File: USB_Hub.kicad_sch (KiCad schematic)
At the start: 48 parts, among them U4 VL822-QFN76, U5 AP7331-10WG-7, Y1 25MHz

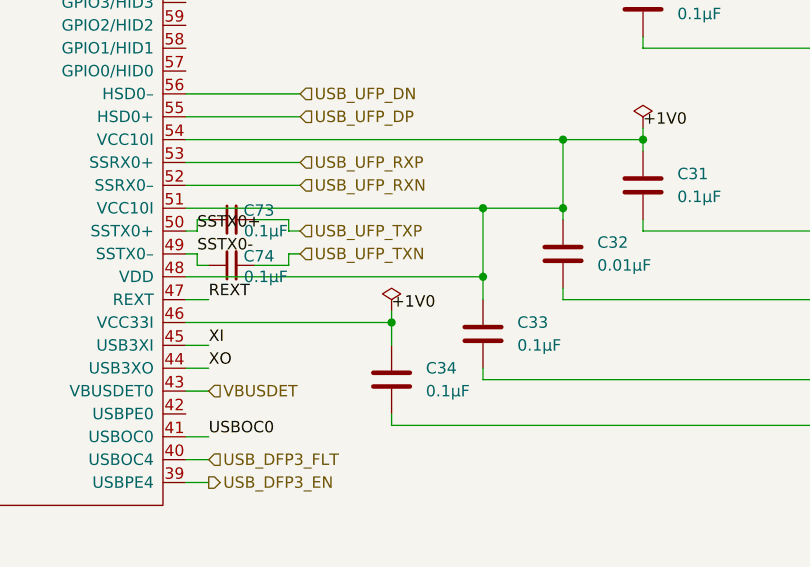
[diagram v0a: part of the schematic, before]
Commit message: Fixed USB Hub wrong net 1V0 -> 3V3
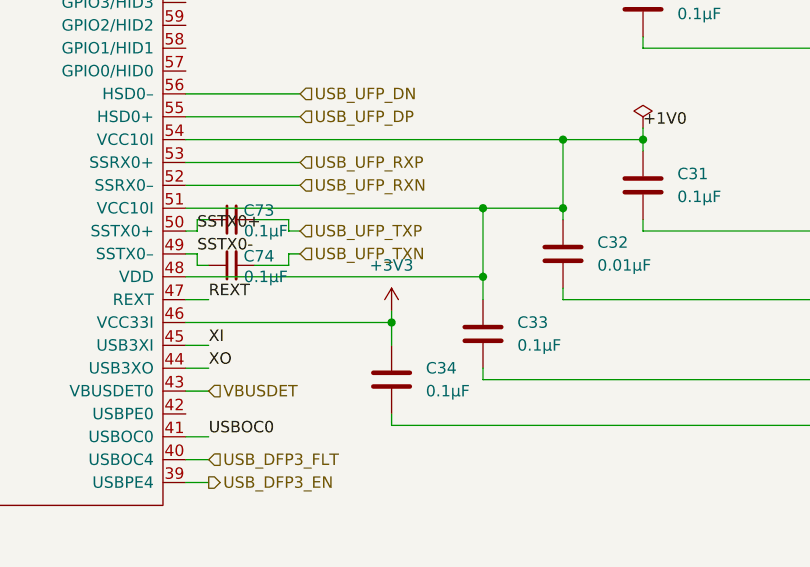
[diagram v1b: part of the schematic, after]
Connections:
- net +1V0: no longer C34.1, U4.46 (VCC33I)
- net +3V3: now also C34.1, U4.46 (VCC33I)
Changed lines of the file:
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@@
 	(wire
 		(pts
-			(xy 175.26 22.86) (xy 177.8 22.86)
-		)
-		(stroke
-			(width 0)
-			(type default)
-		)
-	)
-	(wire
-		(pts
 			(xy 110.49 52.07) (xy 111.76 52.07)
 		)
@@
 	(wire
 		(pts
+			(xy 175.26 22.86) (xy 177.8 22.86)
+		)
+		(stroke
+			(width 0)
+			(type default)
+		)
+	)
+	(wire
+		(pts
 			(xy 175.26 73.66) (xy 187.96 73.66)
 		)
@@
 	)
 	(label "+1V0"
-		(at 198.12 95.25 0)
-		(fields_autoplaced yes)
-		(effects
-			(font
-				(size 1.27 1.27)
-			)
-			(justify left bottom)
-		)
-	)
-	(label "+1V0"
 		(at 20.32 26.67 0)
 		(fields_autoplaced yes)
@@
 		)
 	)
-	(label "USB_DFP3_FLT"
-		(at 166.37 194.31 180)
-		(fields_autoplaced yes)
-		(effects
-			(font
-				(size 1.27 1.27)
-			)
-			(justify right bottom)
-		)
-	)
 	(label "USB_DFP1_FLT"
 		(at 148.59 189.23 180)
@@
 		)
 	)
+	(label "USB_DFP3_FLT"
+		(at 166.37 194.31 180)
+		(fields_autoplaced yes)
+		(effects
+			(font
+				(size 1.27 1.27)
+			)
+			(justify right bottom)
+		)
+	)
 	(label "+1V0"
 		(at 76.2 85.09 0)
@@
 		)
 	)
+	(hierarchical_label "USB_DFP1_FLT"
+		(shape input)
+		(at 177.8 22.86 0)
+		(fields_autoplaced yes)
+		(effects
+			(font
+				(size 1.27 1.27)
+			)
+			(justify left)
+		)
+	)
 	(hierarchical_label "SCL"
 		(shape bidirectional)
@@
 		)
 	)
-	(hierarchical_label "USB_DFP1_FLT"
-		(shape input)
-		(at 177.8 22.86 0)
-		(fields_autoplaced yes)
-		(effects
-			(font
-				(size 1.27 1.27)
-			)
-			(justify left)
-		)
-	)
 	(hierarchical_label "SDA"
 		(shape bidirectional)
@@
 	)
 	(symbol
+		(lib_id "power:+3V3")
+		(at 198.12 95.25 0)
+		(unit 1)
+		(exclude_from_sim no)
+		(in_bom yes)
+		(on_board yes)
+		(dnp no)
+		(fields_autoplaced yes)
+		(property "Reference" "#PWR0129"
+			(at 198.12 99.06 0)
+			(effects
+				(font
+					(size 1.27 1.27)
+				)
+				(hide yes)
+			)
+		)
+		(property "Value" "+3V3"
+			(at 198.12 90.17 0)
+			(effects
+				(font
+					(size 1.27 1.27)
+				)
+			)
+		)
+		(property "Footprint" ""
+			(at 198.12 95.25 0)
+			(effects
+				(font
+					(size 1.27 1.27)
+				)
+				(hide yes)
+			)
+		)
+		(property "Datasheet" ""
+			(at 198.12 95.25 0)
+			(effects
+				(font
+					(size 1.27 1.27)
+				)
+				(hide yes)
+			)
+		)
+		(property "Description" "Power symbol creates a global label with name \"+3V3\""
+			(at 198.12 95.25 0)
+			(effects
+				(font
+					(size 1.27 1.27)
+				)
+				(hide yes)
+			)
+		)
+		(pin "1"
+		)
+		(instances
+			(project "XG_Mobile_Dock"
+				(path "/f97e6956-ab08-42cb-8fed-03fa58e87f0e/ef21a87f-222f-4a81-a291-59975487be1d"
+					(reference "#PWR0129")
+					(unit 1)
+				)
+			)
+		)
+	)
+	(symbol
 		(lib_id "Device:R")
 		(at 266.7 58.42 180)
@@
 					(unit 1)
 				)
-			)
-		)
-	)
-	(symbol
-		(lib_id "power:PWR_FLAG")
-		(at 198.12 95.25 0)
-		(unit 1)
-		(exclude_from_sim no)
-		(in_bom yes)
-		(on_board yes)
-		(dnp no)
-		(fields_autoplaced yes)
-		(property "Reference" "#FLG09"
-			(at 198.12 93.345 0)
-			(effects
-				(font
-					(size 1.27 1.27)
-				)
-				(hide yes)
-			)
-		)
-		(property "Value" "PWR_FLAG"
-			(at 198.12 90.17 0)
-			(effects
-				(font
-					(size 1.27 1.27)
-				)
-				(hide yes)
-			)
-		)
-		(property "Footprint" ""
-			(at 198.12 95.25 0)
-			(effects
-				(font
-					(size 1.27 1.27)
-				)
-				(hide yes)
-			)
-		)
-		(property "Datasheet" "~"
-			(at 198.12 95.25 0)
-			(effects
-				(font
-					(size 1.27 1.27)
-				)
-				(hide yes)
-			)
-		)
-		(property "Description" "Special symbol for telling ERC where power comes from"
-			(at 198.12 95.25 0)
-			(effects
-				(font
-					(size 1.27 1.27)
-				)
-				(hide yes)
-			)
-		)
-		(pin "1"
-		)
-		(instances
-			(project "XG_Mobile_Dock"
-				(path "/f97e6956-ab08-42cb-8fed-03fa58e87f0e/ef21a87f-222f-4a81-a291-59975487be1d"
-					(reference "#FLG09")
-					(unit 1)
-				)

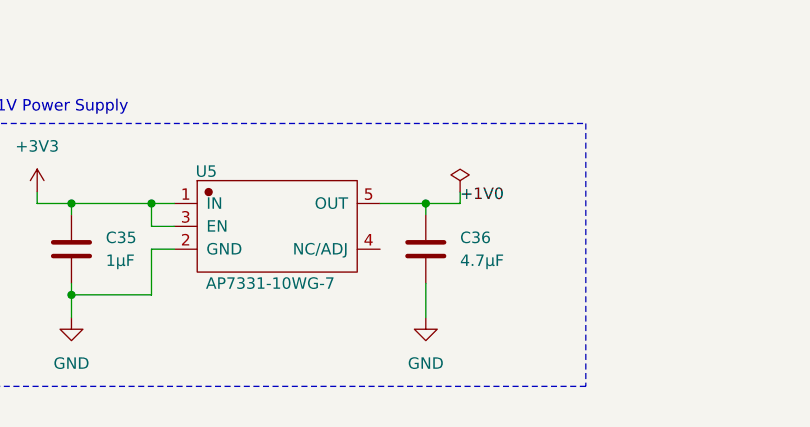
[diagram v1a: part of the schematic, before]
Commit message: Increase thermal mass under 1V0 LDO
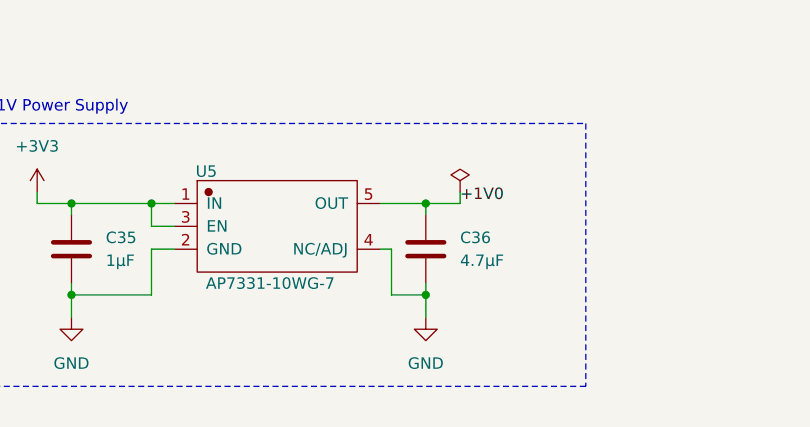
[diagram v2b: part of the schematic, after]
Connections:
- net GND: now also U5.4 (NC/ADJ)
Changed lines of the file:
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@@
 	)
 	(junction
+		(at 66.04 182.88)
+		(diameter 0)
+		(color 0 0 0 0)
+	)
+	(junction
 		(at 41.91 93.98)
 		(diameter 0)
@@
 	(wire
 		(pts
+			(xy 62.23 177.8) (xy 62.23 182.88)
+		)
+		(stroke
+			(width 0)
+			(type default)
+		)
+	)
+	(wire
+		(pts
 			(xy 41.91 109.22) (xy 41.91 110.49)
 		)
@@
 	(wire
 		(pts
-			(xy 66.04 181.61) (xy 66.04 185.42)
+			(xy 66.04 181.61) (xy 66.04 182.88)
 		)
 		(stroke
@@
 	(wire
 		(pts
+			(xy 62.23 182.88) (xy 66.04 182.88)
+		)
+		(stroke
+			(width 0)
+			(type default)
+		)
+	)
+	(wire
+		(pts
 			(xy 208.28 101.6) (xy 208.28 102.87)
 		)
@@
 	(wire
 		(pts
+			(xy 66.04 182.88) (xy 66.04 185.42)
+		)
+		(stroke
+			(width 0)
+			(type default)
+		)
+	)
+	(wire
+		(pts
 			(xy 166.37 173.99) (xy 157.48 173.99)
 		)
@@
 	(wire
 		(pts
+			(xy 60.96 177.8) (xy 62.23 177.8)
+		)
+		(stroke
+			(width 0)
+			(type default)
+		)
+	)
+	(wire
+		(pts
 			(xy 175.26 20.32) (xy 177.8 20.32)
 		)
@@
 		(on_board yes)
 		(dnp no)
-		(fields_autoplaced yes)
 		(property "Reference" "U5"
 			(at 41.656 169.164 0)

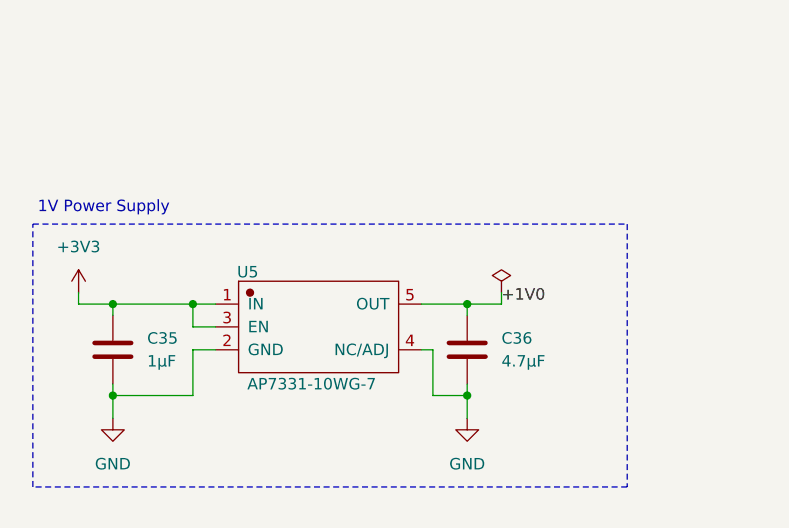
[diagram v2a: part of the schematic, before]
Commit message: Replace AP7331-10WG-7 with AP7361-10ER-13 to handle power draw
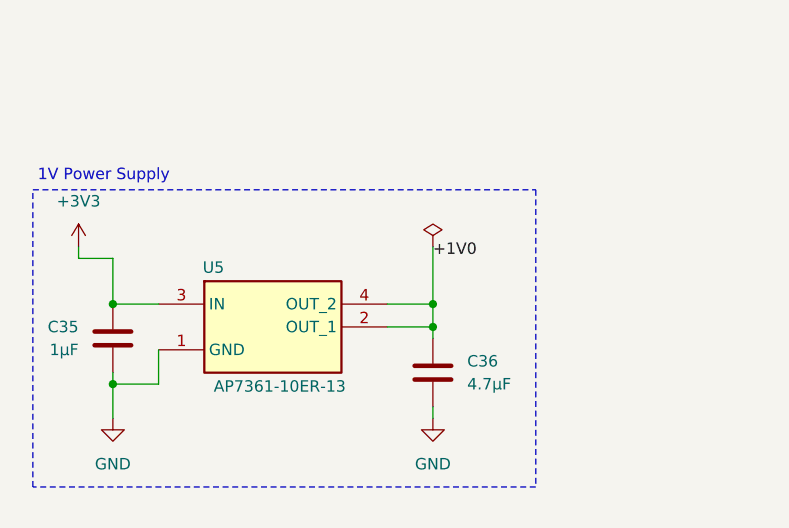
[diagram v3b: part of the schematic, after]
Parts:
- U5: value AP7331-10WG-7 -> AP7361-10ER-13; footprint AP7331-10WG-7:AP7331-10WG-7 -> AP7361-10ER-13:SOT230P700X180-4N; symbol AP7331-10WG-7:AP7331-10WG-7 -> AP7361-10ER-13:AP7361-10ER-13; Height (none) -> 1.8; LCSC C460375 -> C460389; Manufacturer_Name (none) -> Diodes Incorporated; Manufacturer_Part_Number (none) -> AP7361-10ER-13; Mouser Part Number (none) -> 621-AP7361-10ER-13; Mouser Price/Stock (none) -> https://www.mouser.co.uk/ProductDetail/Diodes-Incorporated/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; Part_Number AP7331-10WG-7 -> AP7361-10ER-13; uuid std:bcc43397ad83422c80ea21646716de2d -> (none)
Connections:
- net +1V0: now also U5.2 (OUT_1), U5.4 (OUT_2); no longer U5.5 (OUT)
- net +3V3: no longer U5.1 (IN)
- net GND: now also U5.1 (GND); no longer U5.2 (GND), U5.4 (NC/ADJ)
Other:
- moved on the sheet: C35, C36

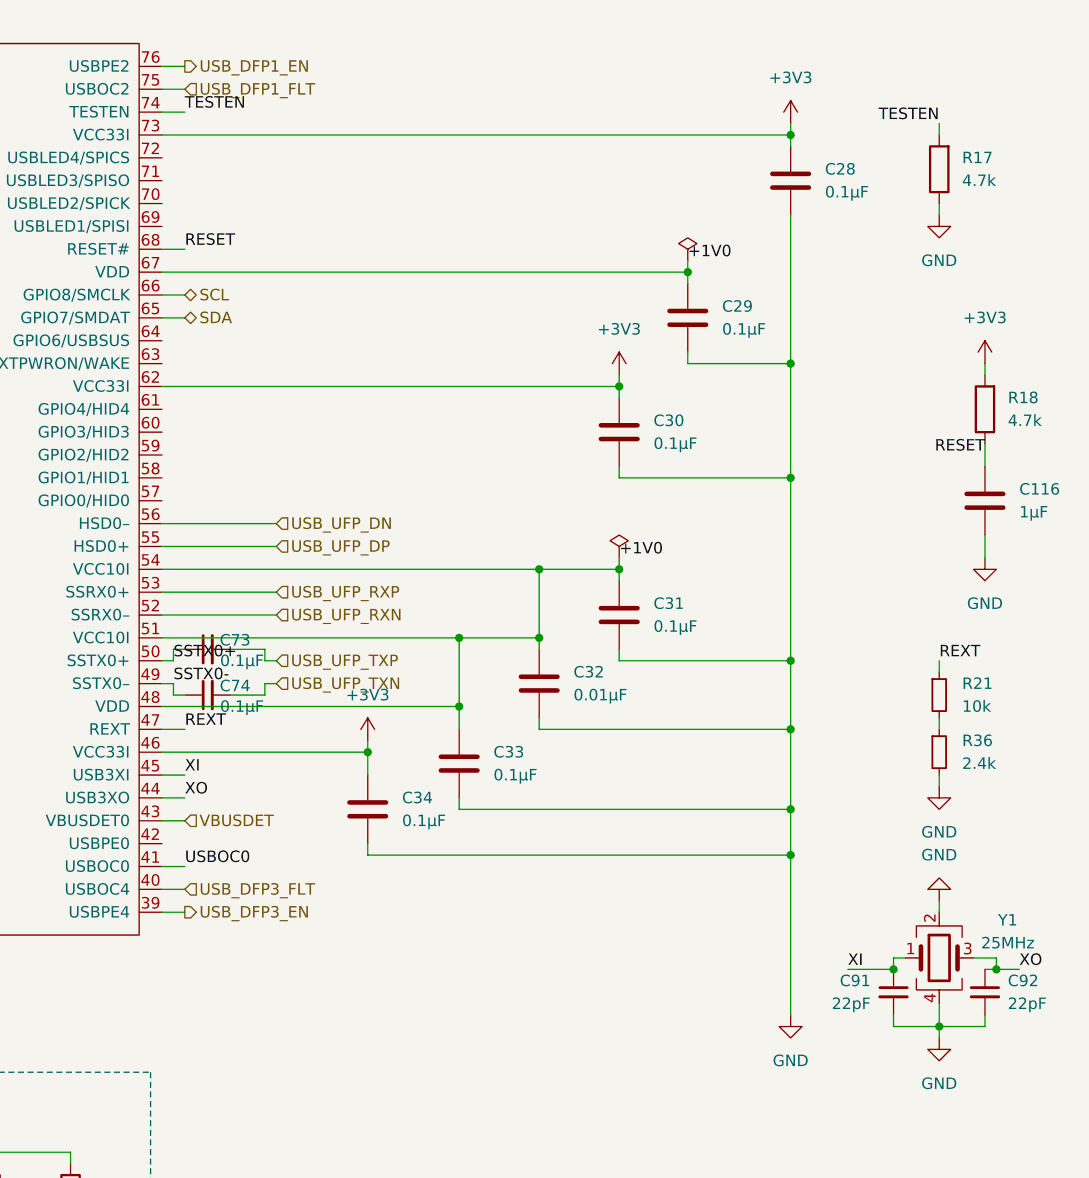
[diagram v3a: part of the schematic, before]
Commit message: pcb: redid layout for USB hub
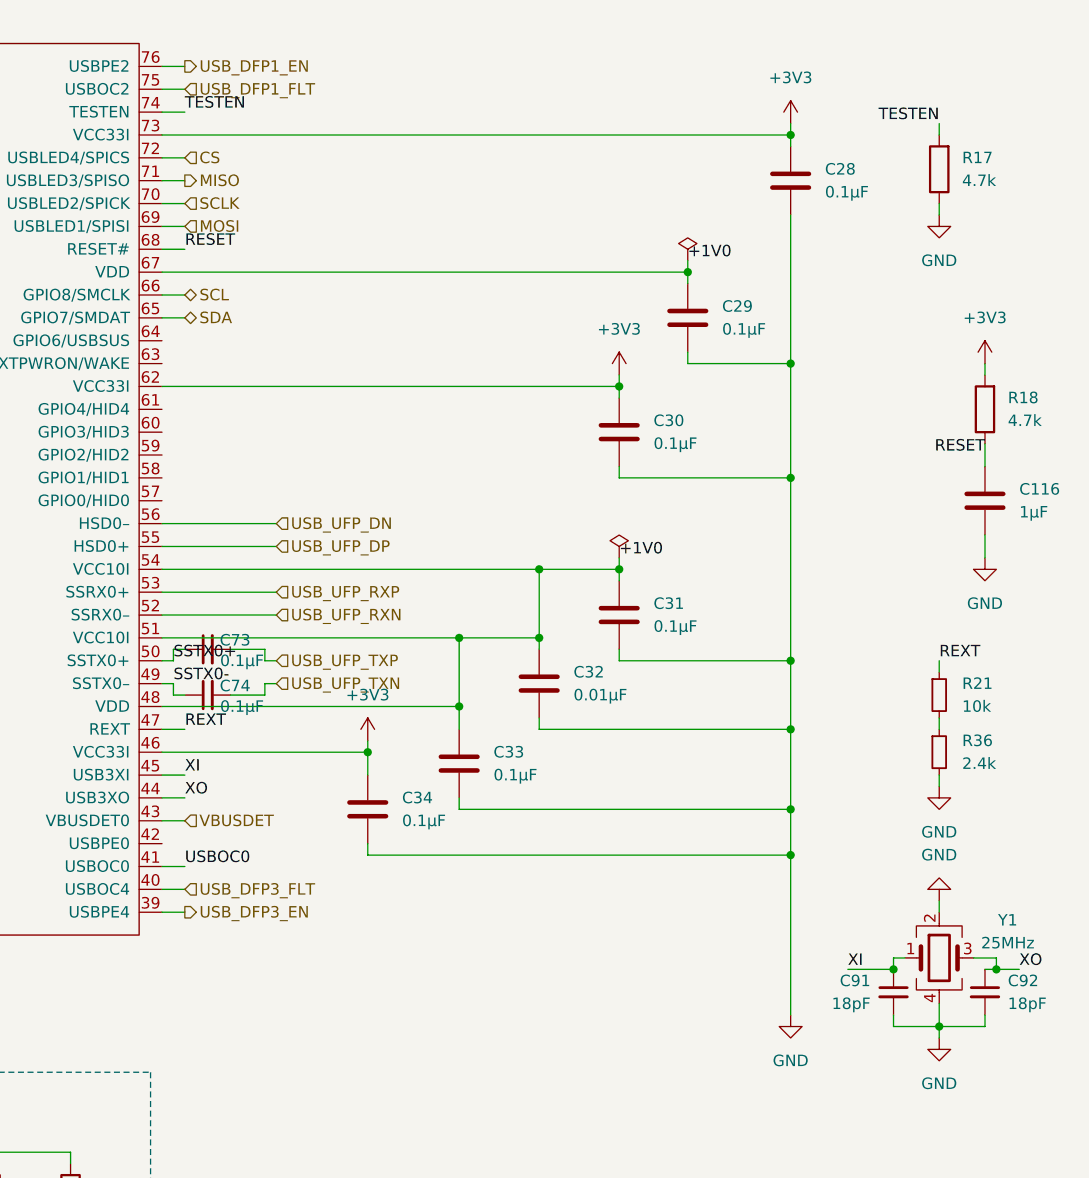
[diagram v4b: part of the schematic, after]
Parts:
- C91, C92: value 22pF -> 18pF; LCSC C1653 -> C1647; Part_Number CL10C220JB8NNNC -> CL10C180JB8NNNC
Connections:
- net MOSI: now reaches U4.69 (USBLED1/SPISI)
- net SCLK: now reaches U4.70 (USBLED2/SPICK)
- net MISO: now reaches U4.71 (USBLED3/SPISO)
- net CS: now reaches U4.72 (USBLED4/SPICS)
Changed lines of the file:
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@@
 	(wire
 		(pts
+			(xy 175.26 33.02) (xy 177.8 33.02)
+		)
+		(stroke
+			(width 0)
+			(type default)
+		)
+	)
+	(wire
+		(pts
 			(xy 156.21 149.86) (xy 156.21 156.21)
 		)
@@
 	(wire
 		(pts
+			(xy 175.26 38.1) (xy 177.8 38.1)
+		)
+		(stroke
+			(width 0)
+			(type default)
+		)
+	)
+	(wire
+		(pts
 			(xy 110.49 99.06) (xy 110.49 100.33)
 		)
@@
 	(wire
 		(pts
+			(xy 175.26 30.48) (xy 177.8 30.48)
+		)
+		(stroke
+			(width 0)
+			(type default)
+		)
+	)
+	(wire
+		(pts
 			(xy 175.26 78.74) (xy 187.96 78.74)
 		)
@@
 	(wire
 		(pts
+			(xy 175.26 35.56) (xy 177.8 35.56)
+		)
+		(stroke
+			(width 0)
+			(type default)
+		)
+	)
+	(wire
+		(pts
 			(xy 261.62 35.56) (xy 261.62 36.83)
 		)
@@
 		)
 	)
+	(hierarchical_label "SCLK"
+		(shape input)
+		(at 177.8 35.56 0)
+		(fields_autoplaced yes)
+		(effects
+			(font
+				(size 1.27 1.27)
+			)
+			(justify left)
+		)
+	)
 	(hierarchical_label "USB_DFP0_DN"
 		(shape input)
@@
 		)
 	)
+	(hierarchical_label "MISO"
+		(shape output)
+		(at 177.8 33.02 0)
+		(fields_autoplaced yes)
+		(effects
+			(font
+				(size 1.27 1.27)
+			)
+			(justify left)
+		)
+	)
+	(hierarchical_label "MOSI"
+		(shape input)
+		(at 177.8 38.1 0)
+		(fields_autoplaced yes)
+		(effects
+			(font
+				(size 1.27 1.27)
+			)
+			(justify left)
+		)
+	)
 	(hierarchical_label "USB_DFP1_DP"
 		(shape input)
@@
 		)
 	)
+	(hierarchical_label "CS"
+		(shape input)
+		(at 177.8 30.48 0)
+		(fields_autoplaced yes)
+		(effects
+			(font
+				(size 1.27 1.27)
+			)
+			(justify left)
+		)
+	)
 	(hierarchical_label "USB_DFP0_EN"
 		(shape output)
@@
 			)
 		)
-		(property "Value" "22pF"
+		(property "Value" "18pF"
 			(at 254 124.4662 0)
 			(effects
@@
 			)
 		)
-		(property "LCSC" "C1653"
+		(property "LCSC" "C1647"
 			(at 256.54 123.19 0)
 			(effects
@@
 			)
 		)
-		(property "Part_Number" "CL10C220JB8NNNC"
+		(property "Part_Number" "CL10C180JB8NNNC"
 			(at 256.54 123.19 0)
 			(effects
@@
 			)
 		)
-		(property "Value" "22pF"
+		(property "Value" "18pF"
 			(at 269.24 124.4662 0)
 			(effects
@@
 			)
 		)
-		(property "LCSC" "C1653"
+		(property "LCSC" "C1647"
 			(at 266.7 123.19 0)
 			(effects
@@
 			)
 		)
-		(property "Part_Number" "CL10C220JB8NNNC"
+		(property "Part_Number" "CL10C180JB8NNNC"
 			(at 266.7 123.19 0)
 			(effects
